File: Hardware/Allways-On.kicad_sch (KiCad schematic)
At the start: 4 parts, among them U1 VS1838B, U2 Arduino_Pro_Micro

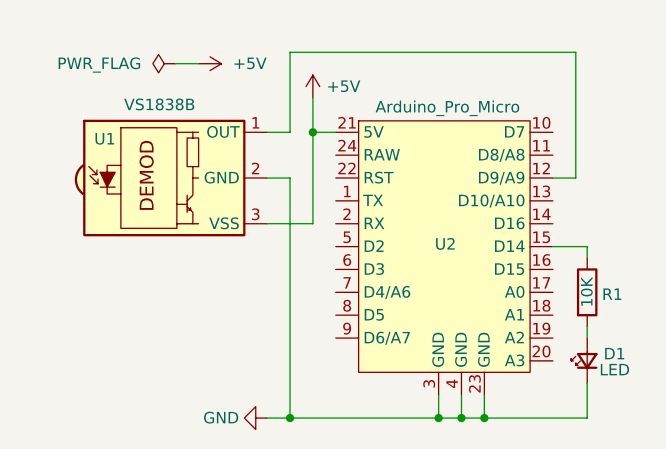
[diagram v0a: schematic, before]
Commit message: Minor fixes on allways-on PCB
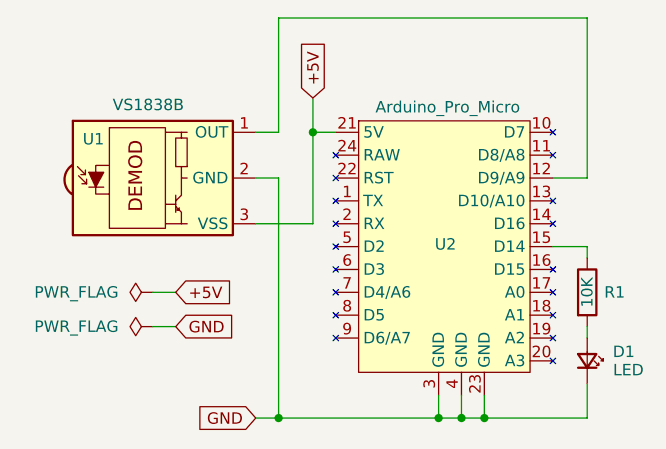
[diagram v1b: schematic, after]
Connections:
- net GND: now reaches D1.1 (K), U1.2 (GND), U2.23 (GND), U2.3 (GND), U2.4 (GND)
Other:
- moved on the sheet: D1, U1
